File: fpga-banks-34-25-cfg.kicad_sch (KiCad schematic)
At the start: 49 parts, among them J13 PinHeader_1x3_P2.54mm_Drill1.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, Q12 2N7002_SOT-23-3, Q13 2N7002_SOT-23-3, Q14 2N7002_SOT-23-3, Q15 2N7002_SOT-23-3, Q16 2N7002_SOT-23-3, U14 XC7A100T-FGG484

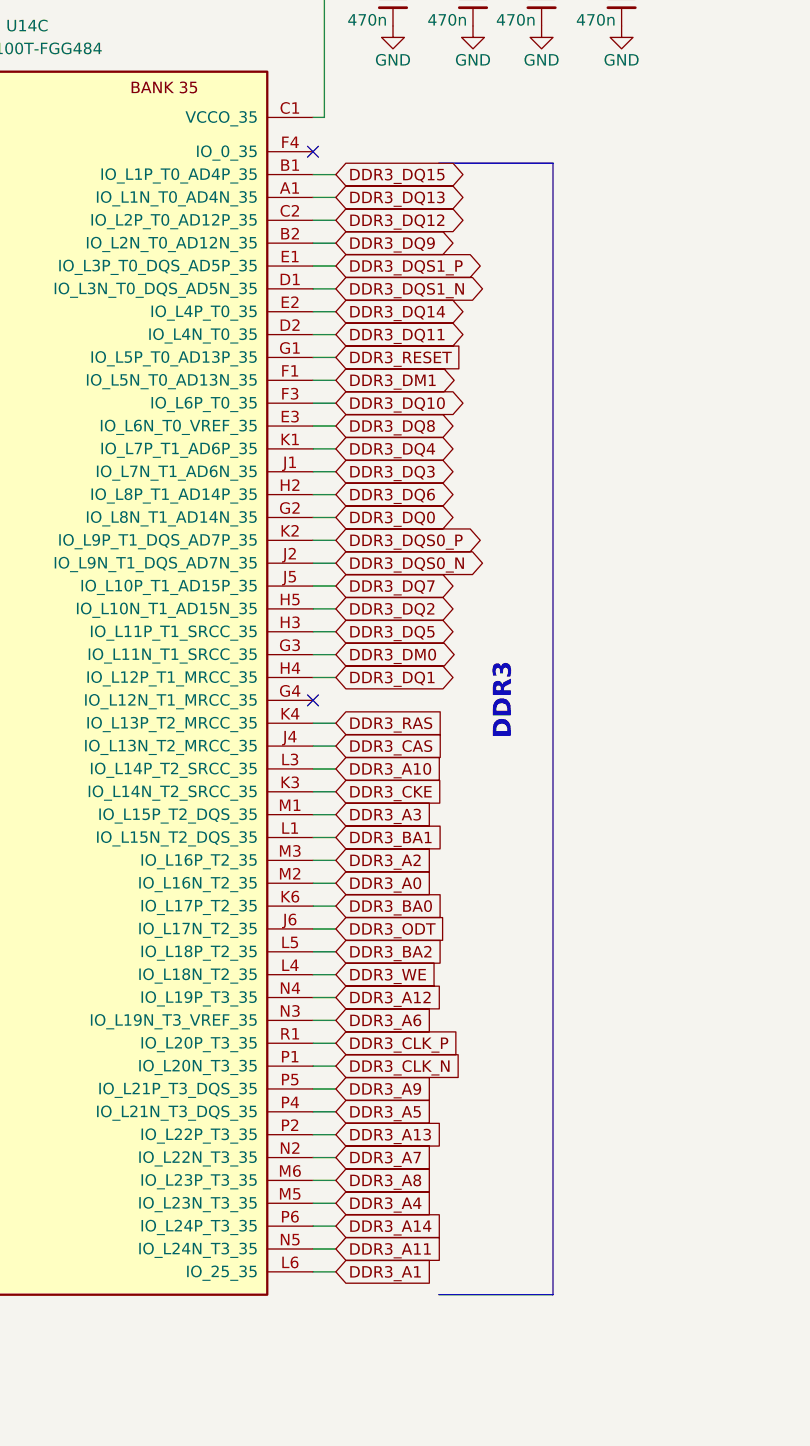
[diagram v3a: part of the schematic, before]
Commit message: All DDR related pins are connected. Continue with the delay matching.
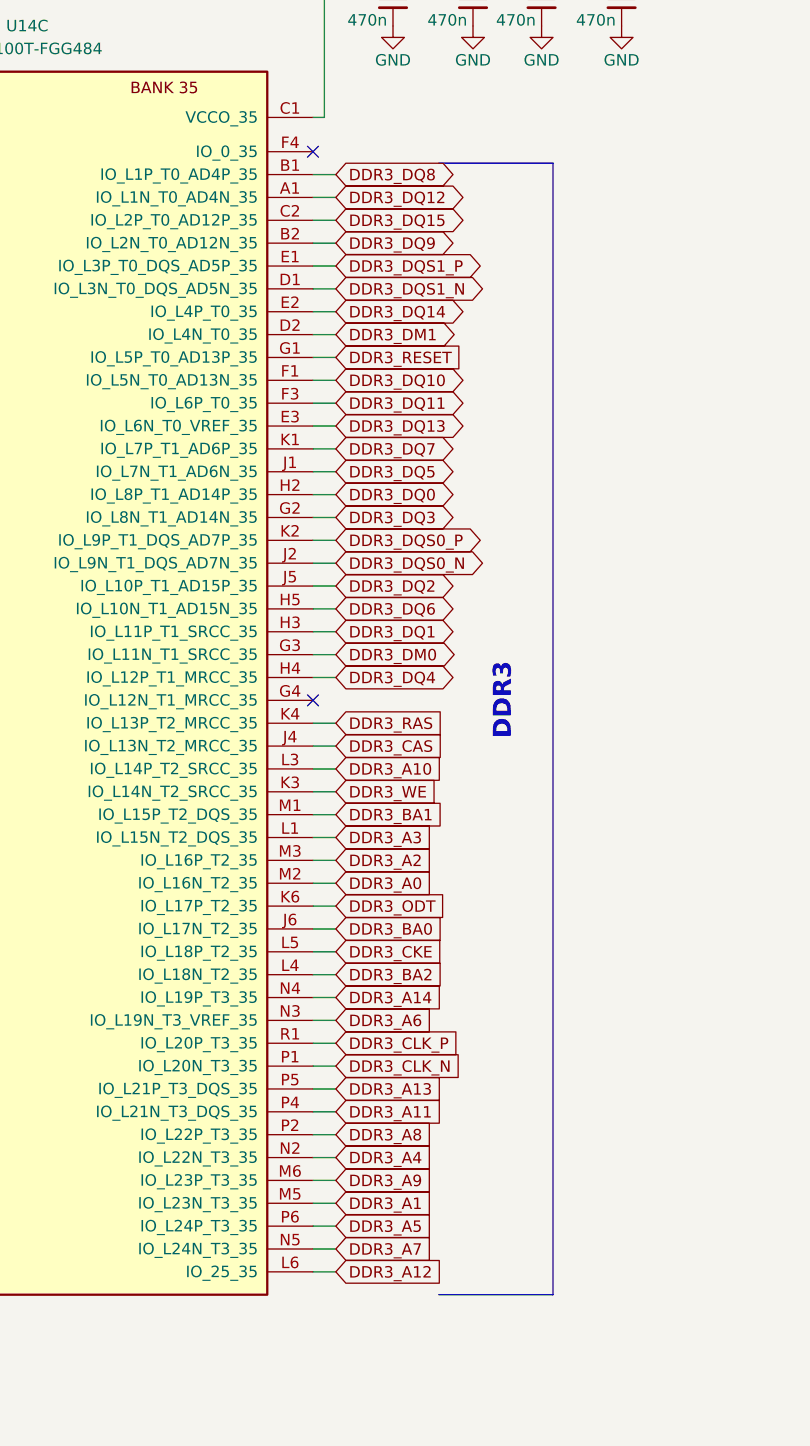
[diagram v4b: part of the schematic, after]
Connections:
- net DDR3_A1: now also U14.M5 (IO_L23N_T3_35); no longer U14.L6 (IO_25_35)
- net DDR3_A11: now also U14.P4 (IO_L21N_T3_DQS_35); no longer U14.N5 (IO_L24N_T3_35)
- net DDR3_A12: now also U14.L6 (IO_25_35); no longer U14.N4 (IO_L19P_T3_35)
- net DDR3_A13: now also U14.P5 (IO_L21P_T3_DQS_35); no longer U14.P2 (IO_L22P_T3_35)
- net DDR3_A14: now also U14.N4 (IO_L19P_T3_35); no longer U14.P6 (IO_L24P_T3_35)
- net DDR3_A3: now also U14.L1 (IO_L15N_T2_DQS_35); no longer U14.M1 (IO_L15P_T2_DQS_35)
- net DDR3_A4: now also U14.N2 (IO_L22N_T3_35); no longer U14.M5 (IO_L23N_T3_35)
- net DDR3_A5: now also U14.P6 (IO_L24P_T3_35); no longer U14.P4 (IO_L21N_T3_DQS_35)
- net DDR3_A7: now also U14.N5 (IO_L24N_T3_35); no longer U14.N2 (IO_L22N_T3_35)
- net DDR3_A8: now also U14.P2 (IO_L22P_T3_35); no longer U14.M6 (IO_L23P_T3_35)
- net DDR3_A9: now also U14.M6 (IO_L23P_T3_35); no longer U14.P5 (IO_L21P_T3_DQS_35)
- net DDR3_BA0: now also U14.J6 (IO_L17N_T2_35); no longer U14.K6 (IO_L17P_T2_35)
- net DDR3_BA1: now also U14.M1 (IO_L15P_T2_DQS_35); no longer U14.L1 (IO_L15N_T2_DQS_35)
- net DDR3_BA2: now also U14.L4 (IO_L18N_T2_35); no longer U14.L5 (IO_L18P_T2_35)
- net DDR3_CKE: now also U14.L5 (IO_L18P_T2_35); no longer U14.K3 (IO_L14N_T2_SRCC_35)
- net DDR3_DM1: now also U14.D2 (IO_L4N_T0_35); no longer U14.F1 (IO_L5N_T0_AD13N_35)
- net DDR3_DQ0: now also U14.H2 (IO_L8P_T1_AD14P_35); no longer U14.G2 (IO_L8N_T1_AD14N_35)
- net DDR3_DQ1: now also U14.H3 (IO_L11P_T1_SRCC_35); no longer U14.H4 (IO_L12P_T1_MRCC_35)
- net DDR3_DQ10: now also U14.F1 (IO_L5N_T0_AD13N_35); no longer U14.F3 (IO_L6P_T0_35)
- net DDR3_DQ11: now also U14.F3 (IO_L6P_T0_35); no longer U14.D2 (IO_L4N_T0_35)
- net DDR3_DQ12: now also U14.A1 (IO_L1N_T0_AD4N_35); no longer U14.C2 (IO_L2P_T0_AD12P_35)
- net DDR3_DQ13: now also U14.E3 (IO_L6N_T0_VREF_35); no longer U14.A1 (IO_L1N_T0_AD4N_35)
- net DDR3_DQ15: now also U14.C2 (IO_L2P_T0_AD12P_35); no longer U14.B1 (IO_L1P_T0_AD4P_35)
- net DDR3_DQ2: now also U14.J5 (IO_L10P_T1_AD15P_35); no longer U14.H5 (IO_L10N_T1_AD15N_35)
- net DDR3_DQ3: now also U14.G2 (IO_L8N_T1_AD14N_35); no longer U14.J1 (IO_L7N_T1_AD6N_35)
- net DDR3_DQ4: now also U14.H4 (IO_L12P_T1_MRCC_35); no longer U14.K1 (IO_L7P_T1_AD6P_35)
- net DDR3_DQ5: now also U14.J1 (IO_L7N_T1_AD6N_35); no longer U14.H3 (IO_L11P_T1_SRCC_35)
- net DDR3_DQ6: now also U14.H5 (IO_L10N_T1_AD15N_35); no longer U14.H2 (IO_L8P_T1_AD14P_35)
- net DDR3_DQ7: now also U14.K1 (IO_L7P_T1_AD6P_35); no longer U14.J5 (IO_L10P_T1_AD15P_35)
- net DDR3_DQ8: now also U14.B1 (IO_L1P_T0_AD4P_35); no longer U14.E3 (IO_L6N_T0_VREF_35)
- net DDR3_ODT: now also U14.K6 (IO_L17P_T2_35); no longer U14.J6 (IO_L17N_T2_35)
- net DDR3_WE: now also U14.K3 (IO_L14N_T2_SRCC_35); no longer U14.L4 (IO_L18N_T2_35)
